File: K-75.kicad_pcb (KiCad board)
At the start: 2 copper layers, 314.3 x 123.8 mm, 177 parts, among them J1 Conn_01x04, SW1 SW_Push, U1 ATmega32U4-AU, Y1 Crystal_GND24_Small

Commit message: Added LEDs
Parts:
- added C10: 0.1uF, Capacitor_SMD:C_0603_1608Metric, B.Cu at (371.9, 163.3)
- added C11: 0.1uF, Capacitor_SMD:C_0603_1608Metric, B.Cu at (372.1, 125.3)
- added C12: 0.1uF, Capacitor_SMD:C_0603_1608Metric, B.Cu at (57.3, 147.2)
- added C13: 0.1uF, Capacitor_SMD:C_0603_1608Metric, B.Cu at (57.1, 181.6)
- added C14: 0.1uF, Capacitor_SMD:C_0603_1608Metric, B.Cu at (372.1, 92.6)
- added C15: 0.1uF, Capacitor_SMD:C_0603_1608Metric, B.Cu at (367.7, 195.2)
- added C8: 0.1uF, Capacitor_SMD:C_0603_1608Metric, B.Cu at (56.0, 80.0)
- added C9: 0.1uF, Capacitor_SMD:C_0603_1608Metric, B.Cu at (57.0, 110.1)
- added D58: WS2812B, LED_SMD:LED_WS2812B_PLCC4_5.0x5.0mm_P3.2mm, B.Cu at (372.1, 84.6)
- added D84: WS2812B, LED_SMD:LED_WS2812B_PLCC4_5.0x5.0mm_P3.2mm, B.Cu at (57.0, 188.8)
- added D85: WS2812B, LED_SMD:LED_WS2812B_PLCC4_5.0x5.0mm_P3.2mm, B.Cu at (372.1, 117.2)
- added D86: WS2812B, LED_SMD:LED_WS2812B_PLCC4_5.0x5.0mm_P3.2mm, B.Cu at (57.1, 155.4)
- added D87: WS2812B, LED_SMD:LED_WS2812B_PLCC4_5.0x5.0mm_P3.2mm, B.Cu at (372.1, 155.4)
- added D88: WS2812B, LED_SMD:LED_WS2812B_PLCC4_5.0x5.0mm_P3.2mm, B.Cu at (57.1, 117.2)
- added D89: WS2812B, LED_SMD:LED_WS2812B_PLCC4_5.0x5.0mm_P3.2mm, B.Cu at (371.6, 188.8)
- added D90: WS2812B, LED_SMD:LED_WS2812B_PLCC4_5.0x5.0mm_P3.2mm, B.Cu at (57.2, 88.3)
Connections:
- U1 pad 10: ROW1 -> COL14
- U1 pad 11: ROW2 -> Net-(U1-Pad11)
- U1 pad 20: Net-(U1-Pad20) -> RGBLED
- U1 pad 8: COL14 -> ROW1
- U1 pad 9: Net-(U1-Pad9) -> ROW2
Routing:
- net GND: track 76.5 -> 630.6 mm, vias 0 -> 2
- net +5V: track 57.2 -> 605.6 mm, vias 3 -> 5
- net Net-(D84-Pad4): track 0.00 -> 323.9 mm
- net Net-(D86-Pad2): track 0.00 -> 44.5 mm
- net ROW1: track 295.3 -> 337.7 mm
- net Net-(D84-Pad2): track 0.00 -> 39.7 mm
- net Net-(D88-Pad2): track 0.00 -> 35.2 mm
- net Net-(D85-Pad2): track 0.00 -> 34.6 mm
- net Net-(D87-Pad2): track 0.00 -> 30.1 mm
- net Net-(D58-Pad2): track 0.00 -> 29.1 mm
- net ROW2: track 290.4 -> 317.3 mm
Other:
- board size 314.3 x 123.8 mm -> 321.9 x 123.8 mm

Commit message: Finished routing
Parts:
- moved C5 1.28 mm to (333.4, 148.7), turned to 270 degrees
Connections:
- D59 pad 1: Net-(D59-Pad1) -> ROW3
- U1 pad 10: COL14 -> RGBLED
- U1 pad 11: Net-(U1-Pad11) -> ROW3
- U1 pad 12: ROW5 -> COL14
- U1 pad 18: ROW4 -> Net-(U1-Pad18)
- U1 pad 19: ROW3 -> Net-(U1-Pad19)
- U1 pad 20: RGBLED -> Net-(U1-Pad20)
- U1 pad 21: Net-(U1-Pad21) -> ROW5
- U1 pad 22: Net-(U1-Pad22) -> ROW4
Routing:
- net RGBLED: track 0.00 -> 94.5 mm
- net ROW5: track 290.1 -> 340.6 mm, vias 0 -> 2
- net ROW3: track 247.7 -> 288.7 mm, vias 0 -> 2
- net ROW4: track 287.6 -> 323.1 mm
- net COL14: track 88.9 -> 100.8 mm
- net +5V: track 605.6 -> 607.1 mm
- net GND: track 630.6 -> 629.9 mm

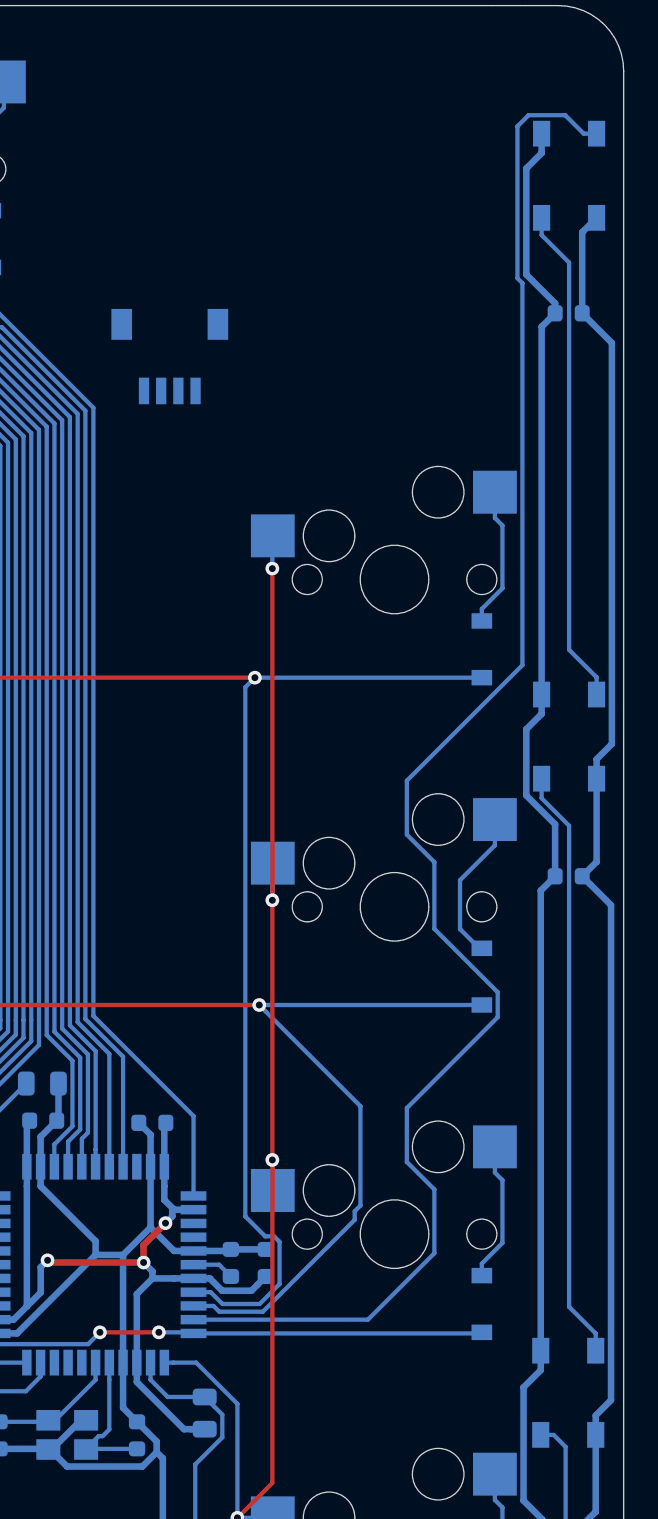
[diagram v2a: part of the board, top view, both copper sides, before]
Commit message: Added USB traces
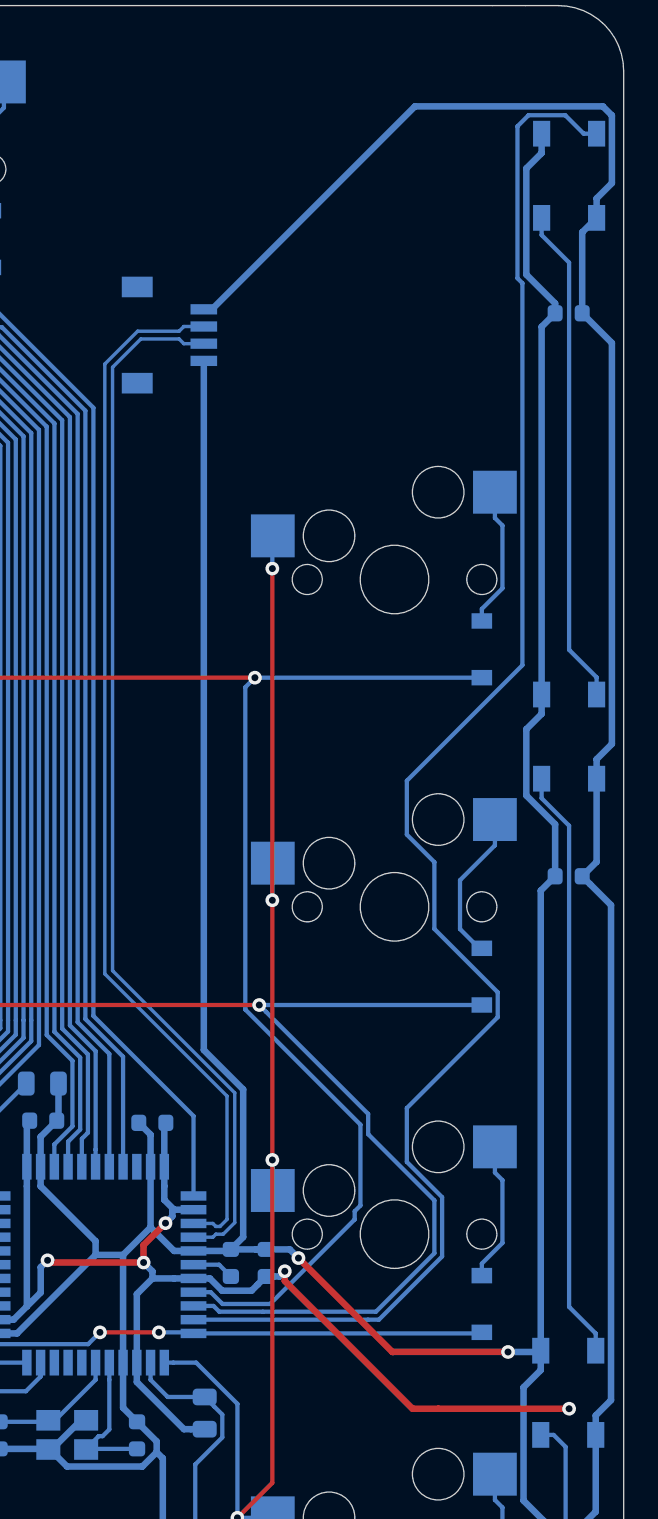
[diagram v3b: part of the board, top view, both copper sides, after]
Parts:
- moved J1 3.18 mm to (346.1, 93.9), turned to 90 degrees
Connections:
- J1 pad 4: VCC -> +5V
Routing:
- net GND: track 629.9 -> 701.9 mm, vias 2 -> 4
- net D-: track 0.00 -> 61.6 mm
- net D+: track 0.00 -> 61.6 mm
- net +5V: track 607.1 -> 664.2 mm, vias 5 -> 7
- net ROW2: track 317.3 -> 324.7 mm
- net ROW1: track 337.7 -> 341.7 mm
- net RGBLED: track 94.5 -> 95.2 mm

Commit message: Finished traces
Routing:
- net +5V: track 664.2 -> 665.9 mm
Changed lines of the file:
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@@
     (thickness 1.6)
     (drawings 746)
-    (tracks 1422)
+    (tracks 1424)
     (zones 0)
     (modules 193)
@@
   (segment (start 374.600501 81.069599) (end 374.600501 85.010499) (width 0.381) (layer B.Cu) (net 5))
   (segment (start 374.600501 85.010499) (end 373.71 85.901) (width 0.381) (layer B.Cu) (net 5))
+  (segment (start 373.266 156.337) (end 372.11 156.337) (width 0.381) (layer B.Cu) (net 5))
+  (segment (start 373.659 156.73) (end 373.266 156.337) (width 0.381) (layer B.Cu) (net 5))
   (segment (start 72.517 80.621) (end 72.517 79.121) (width 0.25) (layer B.Cu) (net 6))
   (segment (start 70.554999 82.583001) (end 72.517 80.621) (width 0.25) (layer B.Cu) (net 6))
@@
   (segment (start 276.606 151.891) (end 295.656 151.891) (width 0.25) (layer B.Cu) (net 54))
   (segment (start 295.656 151.891) (end 326.644 151.891) (width 0.25) (layer B.Cu) (net 54))
-  (via (at 344.805 151.892) (size 0.8) (drill 0.4) (layers F.Cu B.Cu) (net 54))
   (via (at 348.234 151.892) (size 0.8) (drill 0.4) (layers F.Cu B.Cu) (net 54))
   (segment (start 344.805 151.892) (end 348.234 151.892) (width 0.25) (layer F.Cu) (net 54))
-  (segment (start 344.117001 152.579999) (end 344.805 151.892) (width 0.25) (layer B.Cu) (net 54))
-  (segment (start 335.229975 152.579999) (end 344.117001 152.579999) (width 0.25) (layer B.Cu) (net 54))
   (segment (start 326.644 151.891) (end 334.540976 151.891) (width 0.25) (layer B.Cu) (net 54))
   (segment (start 334.540976 151.891) (end 335.229975 152.579999) (width 0.25) (layer B.Cu) (net 54))
@@
   (segment (start 366.966 151.955) (end 367.03 151.891) (width 0.25) (layer B.Cu) (net 54))
   (segment (start 350.251 151.955) (end 366.966 151.955) (width 0.25) (layer B.Cu) (net 54))
+  (segment (start 335.229975 152.579999) (end 344.117001 152.579999) (width 0.25) (layer B.Cu) (net 54))
+  (via (at 344.805 151.892) (size 0.8) (drill 0.4) (layers F.Cu B.Cu) (net 54))
+  (segment (start 344.117001 152.579999) (end 344.805 151.892) (width 0.25) (layer B.Cu) (net 54))
   (segment (start 105.918 142.597) (end 105.918 141.097) (width 0.25) (layer B.Cu) (net 55))
   (segment (start 103.955999 144.559001) (end 105.918 142.597) (width 0.25) (layer B.Cu) (net 55))

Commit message: Fabrication outputs
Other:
- board text added: "K-75"
- board text added: "K-75 Keyboard PCB Rev 1.0 18/4/2022"
- board text added: "Max Uger"
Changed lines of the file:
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@@
   (general
     (thickness 1.6)
-    (drawings 746)
+    (drawings 752)
     (tracks 1424)
     (zones 0)
@@
       (outputformat 1)
       (mirror false)
-      (drillshape 1)
+      (drillshape 0)
       (scaleselection 1)
-      (outputdirectory ""))
+      (outputdirectory "Fabrication Outputs/JLCPCB/"))
   )
   (net 0 "")
@@
     )
   )
+  (gr_text "Max Uger" (at 68.58 194.31) (layer B.SilkS)
+    (effects (font (size 2 2) (thickness 0.2)) (justify mirror))
+  )
+  (gr_text "Max Uger" (at 68.199 194.31) (layer F.SilkS)
+    (effects (font (size 2 2) (thickness 0.2)))
+  )
+  (gr_text "K-75 Keyboard PCB Rev 1.0 18/4/2022" (at 357.632 77.089) (layer B.SilkS)
+    (effects (font (size 1 1) (thickness 0.15)) (justify mirror))
+  )
+  (gr_text K-75 (at 89.408 95.885) (layer B.SilkS)
+    (effects (font (size 8 8) (thickness 0.45)) (justify mirror))
+  )
+  (gr_text K-75 (at 89.408 96.012) (layer F.SilkS)
+    (effects (font (size 8 8) (thickness 0.45)))
+  )
+  (gr_text "K-75 Keyboard PCB Rev 1.0 18/4/2022" (at 357.505 77.089) (layer F.SilkS)
+    (effects (font (size 1 1) (thickness 0.15)))
+  )
   (gr_line (start 60.96 74.676) (end 57.15 74.676) (layer Edge.Cuts) (width 0.05))
